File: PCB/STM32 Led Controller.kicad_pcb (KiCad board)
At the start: 2 copper layers, 107 x 44.2 mm, 66 parts, among them J1 EXT_PWR_CONN, J2 SWD_CONN, J3 USB_C_Receptacle_USB2.0_16P, J4 WS2815, J5 RB1-125BAG1A, J6 Conn_02x04_Top_Bottom, SW1 FSM4JH, U1 Mini360, U2 NCV1117ST33T3G, U3 STM32G0B0RETx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

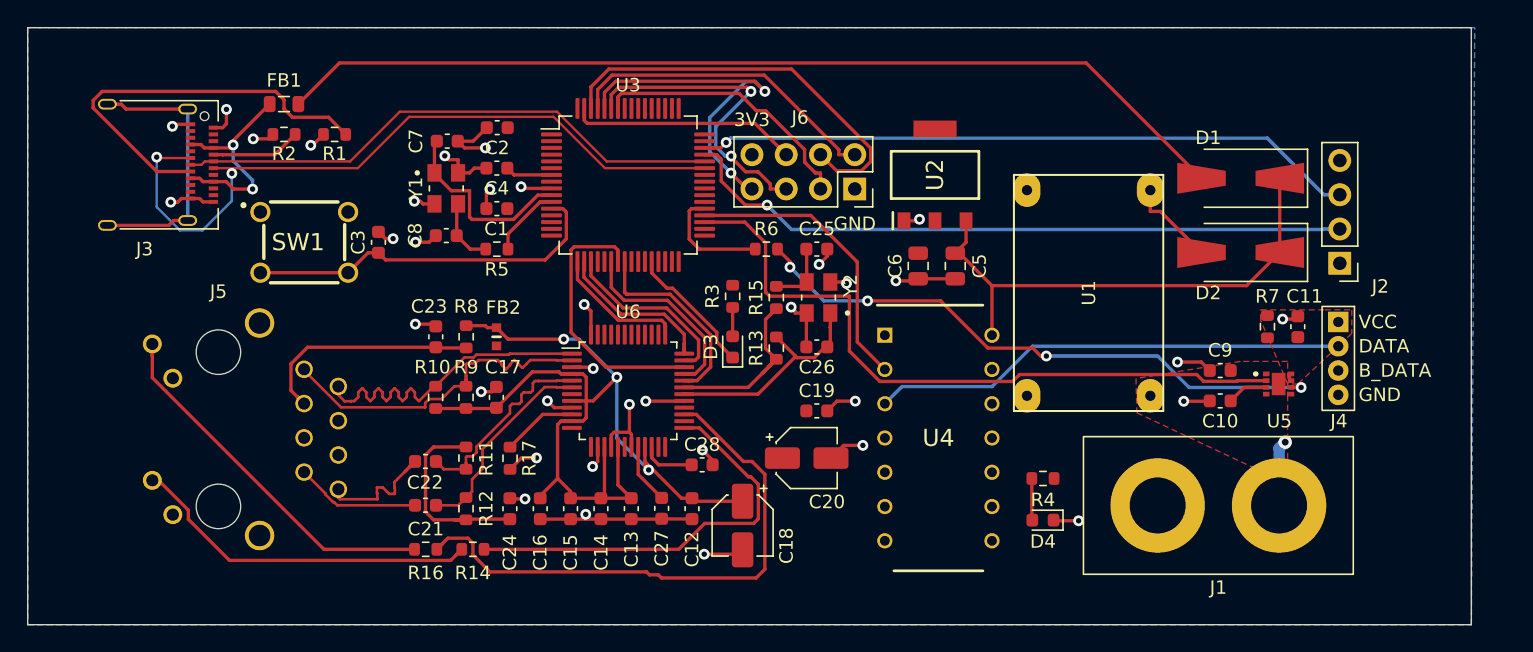
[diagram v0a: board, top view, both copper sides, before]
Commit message: Moved connectors Finished routing Add filleted corners Added name to silkmask Ordered board, REV A complete
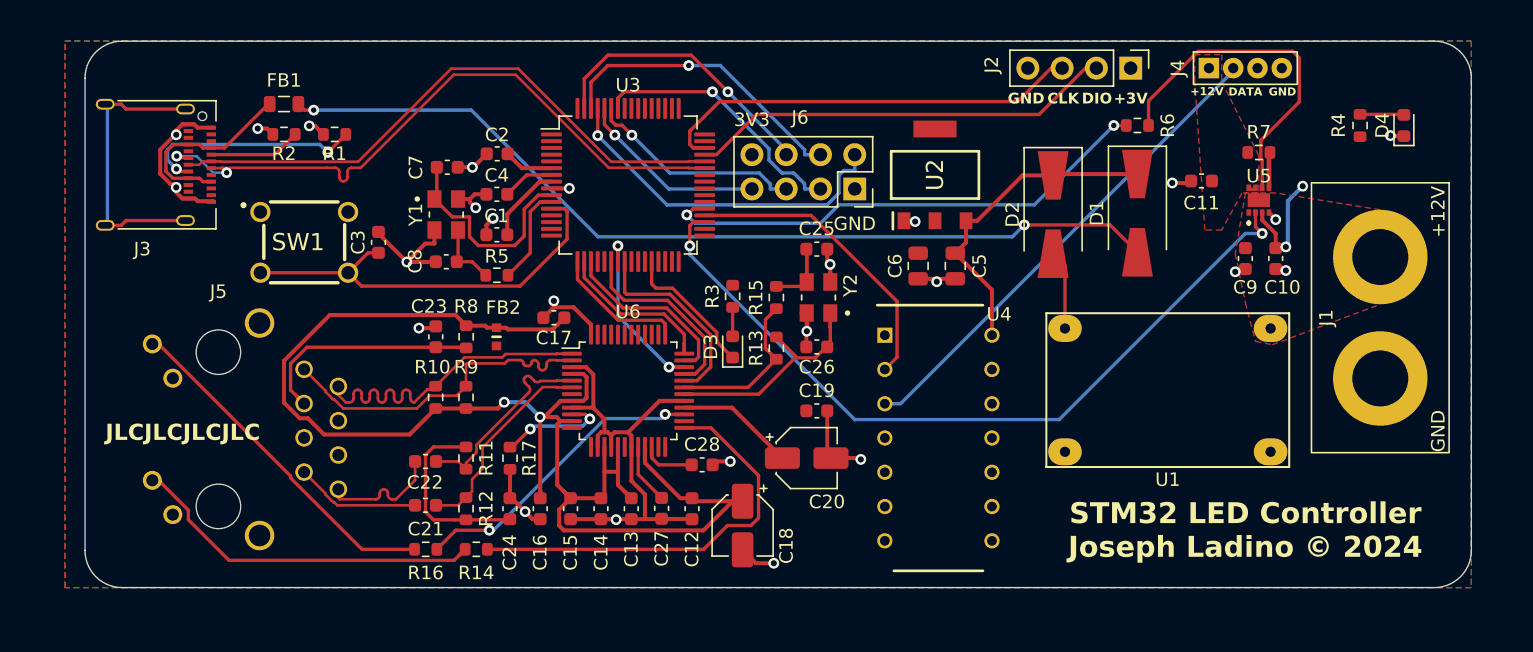
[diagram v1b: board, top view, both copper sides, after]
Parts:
- J3: value USB_C_Receptacle_USB2.0_16P -> 12401610E4-2A
- moved D4 39.6 mm to (217.0, 83.8), turned to 90 degrees
- moved R4 35.2 mm to (213.8, 83.8), turned to 90 degrees
- moved R6 29.0 mm to (197.2, 83.8)
- moved J4 22.7 mm to (205.2, 79.5), turned to 0 degrees
- moved J2 21.2 mm to (196.8, 79.5), turned to -90 degrees
- moved J1 18.4 mm to (215.2, 98.0), turned to -90 degrees
- moved D2 14.2 mm to (191.0, 90.3), turned to -90 degrees
- moved U5 13.7 mm to (206.2, 89.3), turned to 0 degrees
- moved C11 12.9 mm to (202.0, 87.9), turned to 0 degrees
- moved R7 12.9 mm to (206.2, 85.8), turned to 180 degrees
- moved C10 11.3 mm to (207.5, 93.6), turned to 90 degrees
- moved U1 9.29 mm to (199.5, 103.4), turned to 180 degrees
- moved C9 8.51 mm to (205.2, 93.6), turned to 90 degrees
- moved D1 8.08 mm to (197.2, 90.2), turned to -90 degrees
- moved C17 7.28 mm to (154.0, 98.0), turned to 180 degrees
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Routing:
- net +3.3VA: track 73.6 -> 108.6 mm, vias 3 -> 2
- net LED_PWR_OK: track 8.50 -> 37.4 mm, vias 0 -> 2
- net +3V3: track 3.05 -> 27.3 mm, vias 0 -> 2
- net Net-(U6-ACTLED): track 42.1 -> 22.5 mm, vias 0 -> 2
- net STM_SWDIO: track 50.3 -> 31.7 mm, vias 1 -> 0
- net Net-(U5-PG): track 44.0 -> 25.6 mm, vias 4 -> 0
- net STM_SWCLK: track 49.1 -> 31.7 mm, vias 1 -> 0
- net GND: track 91.0 -> 105.0 mm, vias 36 -> 25
- net +5V: track 38.0 -> 24.1 mm
- net Net-(J3-CC2): track 30.4 -> 17.0 mm, vias 0 -> 2
- net ESP_RX: track 26.0 -> 14.1 mm, vias 2 -> 1
- net ESP_EN: track 30.8 -> 22.4 mm, vias 0 -> 1
- net ESP_IO0: track 23.7 -> 16.2 mm, vias 2 -> 1
- net LED_PWR_EN: track 51.5 -> 58.3 mm, vias 0 -> 2
- net USB_D-: track 55.4 -> 49.4 mm
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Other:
- board size 107 x 44.2 mm -> 102.8 x 40.5 mm
- board text added: "+12V"
- board text added: "+3V"
- board text added: "CLK"
- board text added: "DATA"
- board text added: "DIO"
- board text added: "GND"
- board text added: "JLCJLCJLCJLC"
- board text added: "STM32 LED Controller Joseph Ladino️ © 2024"

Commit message: minor tweaks, added logo, adjusted silkscreen
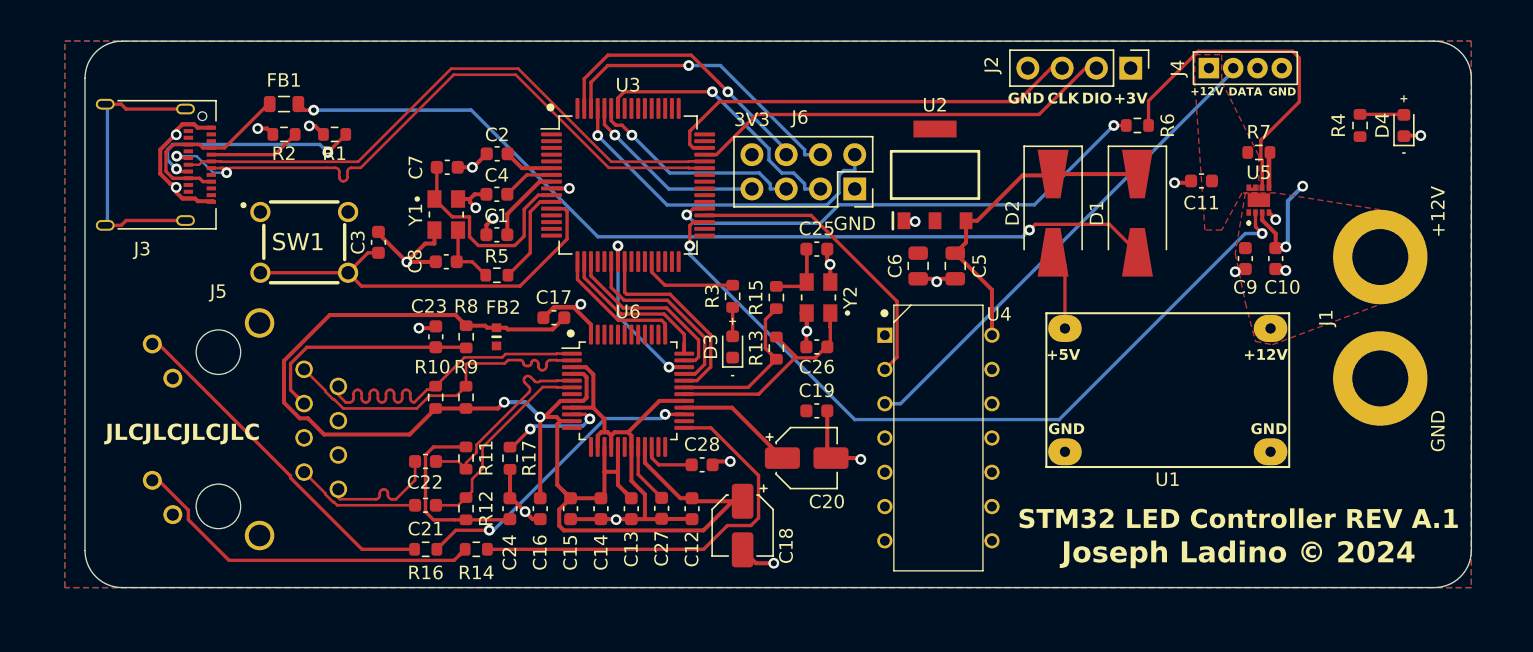
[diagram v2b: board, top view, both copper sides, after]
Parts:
- added svg2mod: G***, Custom:logo, B.Cu at (174.0, 76.6)
- R3, R4: value 100K -> 220
- moved D2 0.10 mm to (191.0, 90.2)
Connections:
- D3 pad 1: /TEST_LED -> GND
- R3 pad 1: +3V3 -> /TEST_LED
- U6 pad 23: unconnected-(U6-RSVD-Pad23) -> GND
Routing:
- net /TEST_LED: track 10.3 -> 7.18 mm
- net GND: track 105.0 -> 106.7 mm
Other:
- board text added: "${REVISION}"
- board text added: "+"
- board text added: "+5V"
- board text added: "-"
- board text added: "Joseph Ladino️ © 2024"
- board text added: "STM32 LED Controller REV A.1"
- board text removed: "STM32 LED Controller Joseph Ladino️ © 2024"

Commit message: tweaked PCB, updated firmware
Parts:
- R3, R4: value 220 -> 330
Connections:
- D3 pad 1: GND -> /TEST_LED
- R3 pad 1: /TEST_LED -> +3V3
- U6 pad 23: GND -> unconnected-(U6-RSVD-Pad23)
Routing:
- net Net-(U5-PG): track 25.6 -> 14.9 mm, vias 0 -> 2
- net /TEST_LED: track 7.18 -> 10.1 mm
- net STM_SWCLK: track 31.7 -> 28.9 mm
- net ESP_EN: track 22.4 -> 20.6 mm
- net ESP_RSTn: track 21.1 -> 19.4 mm
- net +3V3: track 27.3 -> 26.6 mm
- net ESP_TX: track 26.2 -> 25.7 mm
- net LED_PWR_OK: track 37.4 -> 36.8 mm
